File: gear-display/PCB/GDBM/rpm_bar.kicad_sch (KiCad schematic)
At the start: 7 parts, among them J4 Con_Screw_1x04_691313510004

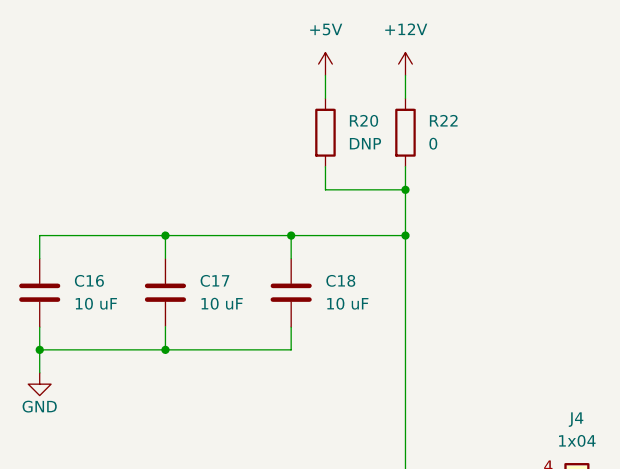
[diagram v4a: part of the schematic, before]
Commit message: PSU and LED powering changed
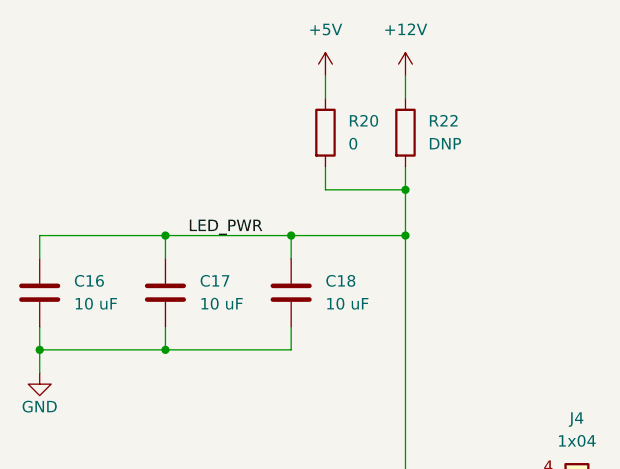
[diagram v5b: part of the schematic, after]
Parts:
- C16, C17, C18: footprint KD_Capacitor:C_1206_3216Metric -> KD_Capacitor:CAPC3216X150N
- R20: value R_0805_DNP -> R_0805_0_automotive; footprint KD_Resistor:RESC2012X60N_DNP -> KD_Resistor:RESC2012X60N; symbol KD_Resistor:R_0805_DNP -> KD_Resistor:R_0805_0_automotive; Code DNP -> 0; DNP T -> F; MFG_PartNo DNP -> RMCF0805ZT0R00; Manufacturer DNP -> Stackpole Electronics Inc; Price 0.00 -> 0.01; Supplier DNP -> Digi-Key; Supplier_PartNo DNP -> RMCF0805ZT0R00CT-ND
- R22: value R_0805_0_automotive -> R_0805_DNP; footprint KD_Resistor:RESC2012X60N -> KD_Resistor:RESC2012X60N_DNP; symbol KD_Resistor:R_0805_0_automotive -> KD_Resistor:R_0805_DNP; Code 0 -> DNP; DNP F -> T; MFG_PartNo RMCF0805ZT0R00 -> DNP; Manufacturer Stackpole Electronics Inc -> DNP; Price 0.01 -> 0.00; Supplier Digi-Key -> DNP; Supplier_PartNo RMCF0805ZT0R00CT-ND -> DNP
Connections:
- net LED_PWR: now reaches C16.1, C17.1, C18.1, J4.4 (Pin_4), R20.2, R22.2
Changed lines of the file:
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@@
     (stroke (width 0) (type default) (color 0 0 0 0))
+  )
+  (label "LED_PWR" (at 128.27 77.47 0)
+    (effects (font (size 1.27 1.27)) (justify left bottom))
   )
   (hierarchical_label "LED_STRIP_B" (shape output) (at 133.35 106.68 180)
@@
     (effects (font (size 1.27 1.27)) (justify right))
   )
-  (symbol (lib_id "KD_Resistor:R_0805_0_automotive") (at 152.4 66.04 0) (unit 1)
+  (symbol (lib_id "KD_Resistor:R_0805_DNP") (at 152.4 66.04 0) (unit 1)
     (in_bom yes) (on_board yes) (fields_autoplaced)
     (property "Reference" "R22" (id 0) (at 154.94 64.7699 0)
       (effects (font (size 1.27 1.27)) (justify left))
     )
-    (property "Value" "R_0805_0_automotive" (id 1) (at 139.7 34.29 0)
-      (effects (font (size 1.27 1.27)) (justify left) hide)
-    )
-    (property "Footprint" "KD_Resistor:RESC2012X60N" (id 2) (at 139.7 52.07 0)
+    (property "Value" "R_0805_DNP" (id 1) (at 139.7 34.29 0)
+      (effects (font (size 1.27 1.27)) (justify left) hide)
+    )
+    (property "Footprint" "KD_Resistor:RESC2012X60N_DNP" (id 2) (at 139.7 52.07 0)
       (effects (font (size 1.27 1.27)) (justify left) hide)
     )
@@
       (effects (font (size 1.27 1.27)) (justify left) hide)
     )
-    (property "Code" "0" (id 4) (at 154.94 67.3099 0)
-      (effects (font (size 1.27 1.27)) (justify left))
-    )
-    (property "Manufacturer" "Stackpole Electronics Inc" (id 5) (at 139.7 36.83 0)
-      (effects (font (size 1.27 1.27)) (justify left) hide)
-    )
-    (property "MFG_PartNo" "RMCF0805ZT0R00" (id 6) (at 139.7 39.37 0)
-      (effects (font (size 1.27 1.27)) (justify left) hide)
-    )
-    (property "Supplier" "Digi-Key" (id 7) (at 139.7 41.91 0)
-      (effects (font (size 1.27 1.27)) (justify left) hide)
-    )
-    (property "Supplier_PartNo" "RMCF0805ZT0R00CT-ND" (id 8) (at 139.7 44.45 0)
-      (effects (font (size 1.27 1.27)) (justify left) hide)
-    )
-    (property "DNP" "F" (id 9) (at 139.7 46.99 0)
-      (effects (font (size 1.27 1.27)) (justify left) hide)
-    )
-    (property "Price" "0.01" (id 10) (at 139.7 49.53 0)
-      (effects (font (size 1.27 1.27)) (justify left) hide)
-    )
-    (pin "1")
-    (pin "2")
-  )
-  (symbol (lib_id "KD_Capacitor:C_1206_10u_50V") (at 111.76 83.82 0) (unit 1)
+    (property "Code" "DNP" (id 4) (at 154.94 67.3099 0)
+      (effects (font (size 1.27 1.27)) (justify left))
+    )
+    (property "Manufacturer" "DNP" (id 5) (at 139.7 36.83 0)
+      (effects (font (size 1.27 1.27)) (justify left) hide)
+    )
+    (property "MFG_PartNo" "DNP" (id 6) (at 139.7 39.37 0)
+      (effects (font (size 1.27 1.27)) (justify left) hide)
+    )
+    (property "Supplier" "DNP" (id 7) (at 139.7 41.91 0)
+      (effects (font (size 1.27 1.27)) (justify left) hide)
+    )
+    (property "Supplier_PartNo" "DNP" (id 8) (at 139.7 44.45 0)
+      (effects (font (size 1.27 1.27)) (justify left) hide)
+    )
+    (property "DNP" "T" (id 9) (at 139.7 46.99 0)
+      (effects (font (size 1.27 1.27)) (justify left) hide)
+    )
+    (property "Price" "0.00" (id 10) (at 139.7 49.53 0)
+      (effects (font (size 1.27 1.27)) (justify left) hide)
+    )
+    (pin "1")
+    (pin "2")
+  )
+  (symbol (lib_name "C_1206_10u_50V_2") (lib_id "KD_Capacitor:C_1206_10u_50V") (at 111.76 83.82 0) (unit 1)
     (in_bom yes) (on_board yes) (fields_autoplaced)
     (property "Reference" "C16" (id 0) (at 115.57 82.5499 0)
@@
       (effects (font (size 1.27 1.27)) (justify left) hide)
     )
-    (property "Footprint" "KD_Capacitor:C_1206_3216Metric" (id 2) (at 99.06 69.85 0)
+    (property "Footprint" "KD_Capacitor:CAPC3216X150N" (id 2) (at 99.06 69.85 0)
       (effects (font (size 1.27 1.27)) (justify left) hide)
     )
@@
     (pin "1")
   )
-  (symbol (lib_id "KD_Capacitor:C_1206_10u_50V") (at 139.7 83.82 0) (unit 1)
+  (symbol (lib_name "C_1206_10u_50V_1") (lib_id "KD_Capacitor:C_1206_10u_50V") (at 139.7 83.82 0) (unit 1)
     (in_bom yes) (on_board yes) (fields_autoplaced)
     (property "Reference" "C18" (id 0) (at 143.51 82.5499 0)
@@
       (effects (font (size 1.27 1.27)) (justify left) hide)
     )
-    (property "Footprint" "KD_Capacitor:C_1206_3216Metric" (id 2) (at 127 69.85 0)
+    (property "Footprint" "KD_Capacitor:CAPC3216X150N" (id 2) (at 127 69.85 0)
       (effects (font (size 1.27 1.27)) (justify left) hide)
     )
@@
     (pin "1")
   )
-  (symbol (lib_id "KD_Resistor:R_0805_DNP") (at 143.51 66.04 0) (unit 1)
+  (symbol (lib_id "KD_Resistor:R_0805_0_automotive") (at 143.51 66.04 0) (unit 1)
     (in_bom yes) (on_board yes) (fields_autoplaced)
     (property "Reference" "R20" (id 0) (at 146.05 64.7699 0)
       (effects (font (size 1.27 1.27)) (justify left))
     )
-    (property "Value" "R_0805_DNP" (id 1) (at 130.81 34.29 0)
-      (effects (font (size 1.27 1.27)) (justify left) hide)
-    )
-    (property "Footprint" "KD_Resistor:RESC2012X60N_DNP" (id 2) (at 130.81 52.07 0)
-      (effects (font (size 1.27 1.27)) (justify left) hide)
-    )
-    (property "Datasheet" "" (id 3) (at 130.81 54.61 0)
-      (effects (font (size 1.27 1.27)) (justify left) hide)
-    )
-    (property "Code" "DNP" (id 4) (at 146.05 67.3099 0)
-      (effects (font (size 1.27 1.27)) (justify left))
-    )
-    (property "Manufacturer" "DNP" (id 5) (at 130.81 36.83 0)
-      (effects (font (size 1.27 1.27)) (justify left) hide)
-    )
-    (property "MFG_PartNo" "DNP" (id 6) (at 130.81 39.37 0)
-      (effects (font (size 1.27 1.27)) (justify left) hide)
-    )
-    (property "Supplier" "DNP" (id 7) (at 130.81 41.91 0)
-      (effects (font (size 1.27 1.27)) (justify left) hide)
-    )
-    (property "Supplier_PartNo" "DNP" (id 8) (at 130.81 44.45 0)
-      (effects (font (size 1.27 1.27)) (justify left) hide)
-    )
-    (property "DNP" "T" (id 9) (at 130.81 46.99 0)
-      (effects (font (size 1.27 1.27)) (justify left) hide)
-    )
-    (property "Price" "0.00" (id 10) (at 130.81 49.53 0)
+    (property "Value" "R_0805_0_automotive" (id 1) (at 130.81 34.29 0)
+      (effects (font (size 1.27 1.27)) (justify left) hide)
+    )
+    (property "Footprint" "KD_Resistor:RESC2012X60N" (id 2) (at 130.81 52.07 0)
+      (effects (font (size 1.27 1.27)) (justify left) hide)
+    )
+    (property "Datasheet" "https://www.seielect.com/catalog/sei-rmcf_rmcp.pdf" (id 3) (at 130.81 54.61 0)
+      (effects (font (size 1.27 1.27)) (justify left) hide)
+    )
+    (property "Code" "0" (id 4) (at 146.05 67.3099 0)
+      (effects (font (size 1.27 1.27)) (justify left))
+    )
+    (property "Manufacturer" "Stackpole Electronics Inc" (id 5) (at 130.81 36.83 0)
+      (effects (font (size 1.27 1.27)) (justify left) hide)
+    )
+    (property "MFG_PartNo" "RMCF0805ZT0R00" (id 6) (at 130.81 39.37 0)
+      (effects (font (size 1.27 1.27)) (justify left) hide)
+    )
+    (property "Supplier" "Digi-Key" (id 7) (at 130.81 41.91 0)
+      (effects (font (size 1.27 1.27)) (justify left) hide)
+    )
+    (property "Supplier_PartNo" "RMCF0805ZT0R00CT-ND" (id 8) (at 130.81 44.45 0)
+      (effects (font (size 1.27 1.27)) (justify left) hide)
+    )
+    (property "DNP" "F" (id 9) (at 130.81 46.99 0)
+      (effects (font (size 1.27 1.27)) (justify left) hide)
+    )
+    (property "Price" "0.01" (id 10) (at 130.81 49.53 0)
       (effects (font (size 1.27 1.27)) (justify left) hide)
     )
@@
       (effects (font (size 1.27 1.27)) (justify left) hide)
     )
-    (property "Footprint" "KD_Capacitor:C_1206_3216Metric" (id 2) (at 113.03 69.85 0)
-      (effects (font (size 1.27 1.27)) (justify left) hide)
-    )
+    (property "Footprint" "KD_Capacitor:CAPC3216X150N" (id 2) (at 113.03 69.85 0)
+      (effects (font (size 1.27 1.27)) (justify left) hide)
+    )

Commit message: layout
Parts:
- C16, C17, C18: symbol KD_Capacitor:C_1206_10u_50V -> KD_Capacitor:C_1206_10u_X5R_50V_automotive; Code 10 uF -> 10u; MFG_PartNo CL31B106KBHNNNE -> GRT31CR61H106ME01L; Manufacturer Samsung Electro-Mechanics -> Murata Electronics; Price 0.10 -> 0.30; Supplier_PartNo 1276-6767-1-ND -> 490-12457-1-ND
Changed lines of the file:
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@@
   (title_block
     (title "Gear Display Board")
-    (date "2022-08-13")
-    (rev "1.0")
+    (date "2023-01-05")
+    (rev "2.0")
     (company "Kallio Designs Oy")
     (comment 1 "Teemu Latonen")
@@
     (pin "2")
   )
-  (symbol (lib_id "KD_Capacitor:C_1206_10u_50V") (at 111.76 83.82 0) (unit 1)
+  (symbol (lib_id "KD_Capacitor:C_1206_10u_X5R_50V_automotive") (at 111.76 83.82 0) (unit 1)
     (in_bom yes) (on_board yes) (fields_autoplaced)
     (property "Reference" "C16" (id 0) (at 115.57 82.5499 0)
@@
       (effects (font (size 1.27 1.27)) (justify left) hide)
     )
-    (property "Datasheet" "datasheet" (id 3) (at 99.06 72.39 0)
-      (effects (font (size 1.27 1.27)) (justify left) hide)
-    )
-    (property "Code" "10 uF" (id 4) (at 115.57 85.0899 0)
-      (effects (font (size 1.27 1.27)) (justify left))
-    )
-    (property "Manufacturer" "Samsung Electro-Mechanics" (id 5) (at 99.06 54.61 0)
-      (effects (font (size 1.27 1.27)) (justify left) hide)
-    )
-    (property "MFG_PartNo" "CL31B106KBHNNNE" (id 6) (at 99.06 57.15 0)
+    (property "Datasheet" "https://search.murata.co.jp/Ceramy/image/img/A01X/G101/ENG/GRT31CR61H106ME01-01.pdf" (id 3) (at 99.06 72.39 0)
+      (effects (font (size 1.27 1.27)) (justify left) hide)
+    )
+    (property "Code" "10u" (id 4) (at 115.57 85.0899 0)
+      (effects (font (size 1.27 1.27)) (justify left))
+    )
+    (property "Manufacturer" "Murata Electronics" (id 5) (at 99.06 54.61 0)
+      (effects (font (size 1.27 1.27)) (justify left) hide)
+    )
+    (property "MFG_PartNo" "GRT31CR61H106ME01L" (id 6) (at 99.06 57.15 0)
       (effects (font (size 1.27 1.27)) (justify left) hide)
     )
@@
       (effects (font (size 1.27 1.27)) (justify left) hide)
     )
-    (property "Supplier_PartNo" "1276-6767-1-ND" (id 8) (at 99.06 62.23 0)
+    (property "Supplier_PartNo" "490-12457-1-ND" (id 8) (at 99.06 62.23 0)
       (effects (font (size 1.27 1.27)) (justify left) hide)
     )
@@
       (effects (font (size 1.27 1.27)) (justify left) hide)
     )
-    (property "Price" "0.10" (id 10) (at 99.06 67.31 0)
+    (property "Price" "0.30" (id 10) (at 99.06 67.31 0)
       (effects (font (size 1.27 1.27)) (justify left) hide)
     )
@@
     (pin "1")
   )
-  (symbol (lib_id "KD_Capacitor:C_1206_10u_50V") (at 139.7 83.82 0) (unit 1)
+  (symbol (lib_id "KD_Capacitor:C_1206_10u_X5R_50V_automotive") (at 139.7 83.82 0) (unit 1)
     (in_bom yes) (on_board yes) (fields_autoplaced)
     (property "Reference" "C18" (id 0) (at 143.51 82.5499 0)
@@
       (effects (font (size 1.27 1.27)) (justify left) hide)
     )
-    (property "Datasheet" "datasheet" (id 3) (at 127 72.39 0)
-      (effects (font (size 1.27 1.27)) (justify left) hide)
-    )
-    (property "Code" "10 uF" (id 4) (at 143.51 85.0899 0)
-      (effects (font (size 1.27 1.27)) (justify left))
-    )
-    (property "Manufacturer" "Samsung Electro-Mechanics" (id 5) (at 127 54.61 0)
-      (effects (font (size 1.27 1.27)) (justify left) hide)
-    )
-    (property "MFG_PartNo" "CL31B106KBHNNNE" (id 6) (at 127 57.15 0)
+    (property "Datasheet" "https://search.murata.co.jp/Ceramy/image/img/A01X/G101/ENG/GRT31CR61H106ME01-01.pdf" (id 3) (at 127 72.39 0)
+      (effects (font (size 1.27 1.27)) (justify left) hide)
+    )
+    (property "Code" "10u" (id 4) (at 143.51 85.0899 0)
+      (effects (font (size 1.27 1.27)) (justify left))
+    )
+    (property "Manufacturer" "Murata Electronics" (id 5) (at 127 54.61 0)
+      (effects (font (size 1.27 1.27)) (justify left) hide)
+    )
+    (property "MFG_PartNo" "GRT31CR61H106ME01L" (id 6) (at 127 57.15 0)
       (effects (font (size 1.27 1.27)) (justify left) hide)
     )
@@
       (effects (font (size 1.27 1.27)) (justify left) hide)
     )
-    (property "Supplier_PartNo" "1276-6767-1-ND" (id 8) (at 127 62.23 0)
+    (property "Supplier_PartNo" "490-12457-1-ND" (id 8) (at 127 62.23 0)
       (effects (font (size 1.27 1.27)) (justify left) hide)
     )
@@
       (effects (font (size 1.27 1.27)) (justify left) hide)
     )
-    (property "Price" "0.10" (id 10) (at 127 67.31 0)
+    (property "Price" "0.30" (id 10) (at 127 67.31 0)
       (effects (font (size 1.27 1.27)) (justify left) hide)
     )
@@
     (pin "1")
   )
-  (symbol (lib_id "KD_Capacitor:C_1206_10u_50V") (at 125.73 83.82 0) (unit 1)
+  (symbol (lib_id "KD_Capacitor:C_1206_10u_X5R_50V_automotive") (at 125.73 83.82 0) (unit 1)
     (in_bom yes) (on_board yes) (fields_autoplaced)
     (property "Reference" "C17" (id 0) (at 129.54 82.5499 0)
@@
       (effects (font (size 1.27 1.27)) (justify left) hide)
     )
-    (property "Datasheet" "datasheet" (id 3) (at 113.03 72.39 0)
-      (effects (font (size 1.27 1.27)) (justify left) hide)
-    )
-    (property "Code" "10 uF" (id 4) (at 129.54 85.0899 0)
-      (effects (font (size 1.27 1.27)) (justify left))
-    )
-    (property "Manufacturer" "Samsung Electro-Mechanics" (id 5) (at 113.03 54.61 0)
-      (effects (font (size 1.27 1.27)) (justify left) hide)
-    )
-    (property "MFG_PartNo" "CL31B106KBHNNNE" (id 6) (at 113.03 57.15 0)
+    (property "Datasheet" "https://search.murata.co.jp/Ceramy/image/img/A01X/G101/ENG/GRT31CR61H106ME01-01.pdf" (id 3) (at 113.03 72.39 0)
+      (effects (font (size 1.27 1.27)) (justify left) hide)
+    )
+    (property "Code" "10u" (id 4) (at 129.54 85.0899 0)
+      (effects (font (size 1.27 1.27)) (justify left))
+    )
+    (property "Manufacturer" "Murata Electronics" (id 5) (at 113.03 54.61 0)
+      (effects (font (size 1.27 1.27)) (justify left) hide)
+    )
+    (property "MFG_PartNo" "GRT31CR61H106ME01L" (id 6) (at 113.03 57.15 0)
       (effects (font (size 1.27 1.27)) (justify left) hide)
     )
@@
       (effects (font (size 1.27 1.27)) (justify left) hide)
     )
-    (property "Supplier_PartNo" "1276-6767-1-ND" (id 8) (at 113.03 62.23 0)
+    (property "Supplier_PartNo" "490-12457-1-ND" (id 8) (at 113.03 62.23 0)
       (effects (font (size 1.27 1.27)) (justify left) hide)
     )
@@
       (effects (font (size 1.27 1.27)) (justify left) hide)
     )
-    (property "Price" "0.10" (id 10) (at 113.03 67.31 0)
-      (effects (font (size 1.27 1.27)) (justify left) hide)
-    )
+    (property "Price" "0.30" (id 10) (at 113.03 67.31 0)
+      (effects (font (size 1.27 1.27)) (justify left) hide)
+    )

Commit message: Added a ferrite and silk screen markings
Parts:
- C16, C17, C18: value C_1206_10u_50V -> C_1206_10u_X5R_50V_automotive
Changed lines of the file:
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@@
       (effects (font (size 1.27 1.27)) (justify left))
     )
-    (property "Value" "C_1206_10u_50V" (id 1) (at 99.06 52.07 0)
+    (property "Value" "C_1206_10u_X5R_50V_automotive" (id 1) (at 99.06 52.07 0)
       (effects (font (size 1.27 1.27)) (justify left) hide)
     )
@@
       (effects (font (size 1.27 1.27)) (justify left))
     )
-    (property "Value" "C_1206_10u_50V" (id 1) (at 127 52.07 0)
+    (property "Value" "C_1206_10u_X5R_50V_automotive" (id 1) (at 127 52.07 0)
       (effects (font (size 1.27 1.27)) (justify left) hide)
     )
@@
       (effects (font (size 1.27 1.27)) (justify left))
     )
-    (property "Value" "C_1206_10u_50V" (id 1) (at 113.03 52.07 0)
-      (effects (font (size 1.27 1.27)) (justify left) hide)
-    )
+    (property "Value" "C_1206_10u_X5R_50V_automotive" (id 1) (at 113.03 52.07 0)
+      (effects (font (size 1.27 1.27)) (justify left) hide)
+    )
